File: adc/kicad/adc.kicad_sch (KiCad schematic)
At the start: 115 parts, among them J1 Conn_01x07_Pin, J2 Conn_01x02_Pin, J3 Conn_01x02_Pin, J4 Conn_01x02_Pin, J5 pcie_98, U1 ADS1261BIRHBT, U2 ESD5344D-TP, U3 TPS7A2050PDBVR, U4 TPS7A2025PDBVRr, U6 TPS65135, U7 ADP7182AUJZ-5.0, U8 ADP7182AUJZ-2.5, U9 XC6206P332MR

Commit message: Replaced ADC DC/DC inductor with a higher current one.
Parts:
- L1: footprint Inductor_SMD:L_0805_2012Metric -> adc:Inductor_C329578; LCSC C531291 -> C329578
- R23, R24: value 5K1 -> 10K; LCSC C25905 -> C25744
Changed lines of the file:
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@@
       (effects (font (size 1.27 1.27)))
     )
-    (property "Value" "5K1" (at 269.24 113.665 0)
+    (property "Value" "10K" (at 269.24 113.665 0)
       (effects (font (size 1.27 1.27)))
     )
@@
       (effects (font (size 1.27 1.27)) hide)
     )
-    (property "LCSC" "C25905" (at 272.415 112.395 0)
+    (property "LCSC" "C25744" (at 272.415 112.395 0)
       (effects (font (size 1.27 1.27)) hide)
     )
@@
       (effects (font (size 1.27 1.27)))
     )
-    (property "Value" "5K1" (at 287.02 113.665 0)
+    (property "Value" "10K" (at 287.02 113.665 0)
       (effects (font (size 1.27 1.27)))
     )
@@
       (effects (font (size 1.27 1.27)) hide)
     )
-    (property "LCSC" "C25905" (at 290.195 112.395 0)
+    (property "LCSC" "C25744" (at 290.195 112.395 0)
       (effects (font (size 1.27 1.27)) hide)
     )
@@
       (effects (font (size 1.27 1.27)))
     )
-    (property "Footprint" "Inductor_SMD:L_0805_2012Metric" (at 62.23 177.8 0)
+    (property "Footprint" "adc:Inductor_C329578" (at 62.23 177.8 0)
       (effects (font (size 1.27 1.27)) hide)
     )
@@
       (effects (font (size 1.27 1.27)) hide)
     )
-    (property "LCSC" "C531291" (at 62.23 177.8 90)
-      (effects (font (size 1.27 1.27)) hide)
-    )
+    (property "LCSC" "C329578" (at 62.23 177.8 90)
+      (effects (font (size 1.27 1.27)) hide)
+    )

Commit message: Updated JLCPCB part info and rotations.
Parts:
- J2, J3, J4, U7, U8, U9: JLCRotOffset (none) -> 180
- R31: LCSC C2759490 -> C4008631
- R33: LCSC C172084 -> C1861540
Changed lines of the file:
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@@
       (effects (font (size 1.27 1.27)) hide)
     )
-    (property "LCSC" "C2759490" (at 80.645 198.755 0)
+    (property "LCSC" "C4008631" (at 80.645 198.755 0)
       (effects (font (size 1.27 1.27)) hide)
     )
@@
       (effects (font (size 1.27 1.27)) hide)
     )
+    (property "JLCRotOffset" "180" (at 153.67 219.71 0)
+      (effects (font (size 1.27 1.27)) hide)
+    )
     (pin "1")
     (pin "2")
@@
       (effects (font (size 1.27 1.27)))
     )
+    (property "JLCRotOffset" "180" (at 284.48 186.69 0)
+      (effects (font (size 1.27 1.27)) hide)
+    )
     (pin "1")
     (pin "2")
@@
       (effects (font (size 1.27 1.27)) hide)
     )
-    (property "LCSC" "C172084" (at 80.645 213.36 0)
+    (property "LCSC" "C1861540" (at 80.645 213.36 0)
       (effects (font (size 1.27 1.27)) hide)
     )
@@
       (effects (font (size 1.27 1.27)) hide)
     )
+    (property "JLCRotOffset" "180" (at 187.96 48.895 0)
+      (effects (font (size 1.27 1.27)) hide)
+    )
     (pin "1")
     (pin "2")
@@
       (effects (font (size 1.27 1.27)) hide)
     )
+    (property "JLCRotOffset" "180" (at 124.46 48.895 0)
+      (effects (font (size 1.27 1.27)) hide)
+    )
     (pin "1")
     (pin "2")
@@
       (effects (font (size 1.27 1.27)) hide)
     )
+    (property "JLCRotOffset" "180" (at 250.825 48.895 0)
+      (effects (font (size 1.27 1.27)) hide)
+    )
     (pin "1")
     (pin "2")
@@
       (effects (font (size 1.27 1.27)) hide)
     )
+    (property "JLCRotOffset" "180" (at 201.295 219.71 0)
+      (effects (font (size 1.27 1.27)) hide)
+    )

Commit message: Fixed library pathes and bus pin number.
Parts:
- R33: LCSC C1861540 -> C4035752
- TP1, TP2, TP3, TP4, TP5, TP6, TP7, TP8, TP9: symbol Connector:TestPoint -> common:TestPoint
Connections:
- net PB14: now also J5.A16 (Pin_a16); no longer J5.B14 (Pin_b14)
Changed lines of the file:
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@@
   (no_connect (at 347.345 184.15))
   (no_connect (at 334.645 153.67))
-  (no_connect (at 347.345 100.33))
+  (no_connect (at 334.645 95.25))
   (no_connect (at 347.345 171.45))
   (no_connect (at 78.74 79.375))
@@
     (stroke (width 0) (type default))
   )
-  (wire (pts (xy 323.215 95.25) (xy 334.645 95.25))
+  (wire (pts (xy 347.345 100.33) (xy 357.505 100.33))
     (stroke (width 0) (type default))
   )
@@
     (effects (font (size 1.27 1.27)) (justify left bottom))
   )
-  (label "PB14" (at 323.215 95.25 0) (fields_autoplaced)
-    (effects (font (size 1.27 1.27)) (justify left bottom))
+  (label "PB14" (at 357.505 100.33 180) (fields_autoplaced)
+    (effects (font (size 1.27 1.27)) (justify right bottom))
   )
   (label "-2V5A" (at 55.88 149.86 90) (fields_autoplaced)
@@
     )
   )
-  (symbol (lib_id "Connector:TestPoint") (at 227.33 170.18 0) (unit 1)
+  (symbol (lib_id "common:TestPoint") (at 227.33 170.18 0) (unit 1)
     (in_bom no) (on_board yes) (dnp no)
     (property "Reference" "TP7" (at 226.06 164.465 0)
@@
       (effects (font (size 1.27 1.27)) hide)
     )
-    (property "LCSC" "C1861540" (at 80.645 213.36 0)
+    (property "LCSC" "C4035752" (at 80.645 213.36 0)
       (effects (font (size 1.27 1.27)) hide)
     )
@@
     )
   )
-  (symbol (lib_id "Connector:TestPoint") (at 227.33 222.25 180) (unit 1)
+  (symbol (lib_id "common:TestPoint") (at 227.33 222.25 180) (unit 1)
     (in_bom no) (on_board yes) (dnp no)
     (property "Reference" "TP8" (at 228.6 227.965 0)
@@
     )
   )
-  (symbol (lib_id "Connector:TestPoint") (at 33.655 193.675 0) (unit 1)
+  (symbol (lib_id "common:TestPoint") (at 33.655 193.675 0) (unit 1)
     (in_bom no) (on_board yes) (dnp no)
     (property "Reference" "TP2" (at 32.385 187.96 0)
@@
     )
   )
-  (symbol (lib_id "Connector:TestPoint") (at 93.98 218.44 180) (unit 1)
+  (symbol (lib_id "common:TestPoint") (at 93.98 218.44 180) (unit 1)
     (in_bom no) (on_board yes) (dnp no)
     (property "Reference" "TP4" (at 95.25 224.155 0)
@@
     )
   )
-  (symbol (lib_id "Connector:TestPoint") (at 299.72 184.15 0) (unit 1)
+  (symbol (lib_id "common:TestPoint") (at 299.72 184.15 0) (unit 1)
     (in_bom no) (on_board yes) (dnp no)
     (property "Reference" "TP9" (at 298.45 178.435 0)
@@
     )
   )
-  (symbol (lib_id "Connector:TestPoint") (at 174.625 222.25 180) (unit 1)
+  (symbol (lib_id "common:TestPoint") (at 174.625 222.25 180) (unit 1)
     (in_bom no) (on_board yes) (dnp no)
     (property "Reference" "TP6" (at 175.895 227.965 0)
@@
     )
   )
-  (symbol (lib_id "Connector:TestPoint") (at 259.715 155.575 0) (unit 1)
+  (symbol (lib_id "common:TestPoint") (at 259.715 155.575 0) (unit 1)
     (in_bom no) (on_board yes) (dnp no)
     (property "Reference" "TP1" (at 258.445 149.86 0)
@@
     )
   )
-  (symbol (lib_id "Connector:TestPoint") (at 174.625 170.18 0) (unit 1)
+  (symbol (lib_id "common:TestPoint") (at 174.625 170.18 0) (unit 1)
     (in_bom no) (on_board yes) (dnp no)
     (property "Reference" "TP5" (at 173.355 164.465 0)
@@
     )
   )
-  (symbol (lib_id "Connector:TestPoint") (at 93.98 194.31 0) (unit 1)
+  (symbol (lib_id "common:TestPoint") (at 93.98 194.31 0) (unit 1)
     (in_bom no) (on_board yes) (dnp no)
     (property "Reference" "TP3" (at 92.71 188.595 0)

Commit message: Changed LED to green and used DC/DC footprint with longer pads for manual soldering.
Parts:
- D1, D2, D3, D4, D5: LCSC C2286 -> C72043
- U6: footprint Package_DFN_QFN:WQFN-16-1EP_3x3mm_P0.5mm_EP1.68x1.68mm_ThermalVias -> adc:WQFN-16-1EP_3x3mm_P0.5mm_EP1.68x1.68mm_ThermalVias
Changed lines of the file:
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@@
       (effects (font (size 1.27 1.27)) hide)
     )
-    (property "LCSC" "C2286" (at 299.72 121.285 0)
+    (property "LCSC" "C72043" (at 299.72 121.285 0)
       (effects (font (size 1.27 1.27)) hide)
     )
@@
       (effects (font (size 1.27 1.27)) hide)
     )
-    (property "LCSC" "C2286" (at 290.195 121.285 0)
+    (property "LCSC" "C72043" (at 290.195 121.285 0)
       (effects (font (size 1.27 1.27)) hide)
     )
@@
       (effects (font (size 1.27 1.27)))
     )
-    (property "Footprint" "Package_DFN_QFN:WQFN-16-1EP_3x3mm_P0.5mm_EP1.68x1.68mm_ThermalVias" (at 39.37 166.37 0)
+    (property "Footprint" "adc:WQFN-16-1EP_3x3mm_P0.5mm_EP1.68x1.68mm_ThermalVias" (at 39.37 166.37 0)
       (effects (font (size 1.27 1.27)) hide)
     )
@@
       (effects (font (size 1.27 1.27)) hide)
     )
-    (property "LCSC" "C2286" (at 272.415 120.015 0)
+    (property "LCSC" "C72043" (at 272.415 120.015 0)
       (effects (font (size 1.27 1.27)) hide)
     )
@@
       (effects (font (size 1.27 1.27)) hide)
     )
-    (property "LCSC" "C2286" (at 263.525 120.015 0)
+    (property "LCSC" "C72043" (at 263.525 120.015 0)
       (effects (font (size 1.27 1.27)) hide)
     )
@@
       (effects (font (size 1.27 1.27)) hide)
     )
-    (property "LCSC" "C2286" (at 281.305 120.015 0)
+    (property "LCSC" "C72043" (at 281.305 120.015 0)
       (effects (font (size 1.27 1.27)) hide)
     )

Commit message: Changed ADC LEDs values from RED to GRN.
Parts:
- D1, D2, D3, D4, D5: value RED -> GRN
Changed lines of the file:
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@@
       (effects (font (size 1.27 1.27)) (justify right))
     )
-    (property "Value" "RED" (at 305.435 118.745 90)
+    (property "Value" "GRN" (at 305.435 118.745 90)
       (effects (font (size 1.27 1.27)) (justify right))
     )
@@
       (effects (font (size 1.27 1.27)) (justify right))
     )
-    (property "Value" "RED" (at 295.91 118.745 90)
+    (property "Value" "GRN" (at 295.91 118.745 90)
       (effects (font (size 1.27 1.27)) (justify right))
     )
@@
       (effects (font (size 1.27 1.27)) (justify right))
     )
-    (property "Value" "RED" (at 266.7 122.555 90)
+    (property "Value" "GRN" (at 266.7 122.555 90)
       (effects (font (size 1.27 1.27)) (justify right))
     )
@@
       (effects (font (size 1.27 1.27)) (justify right))
     )
-    (property "Value" "RED" (at 257.81 122.555 90)
+    (property "Value" "GRN" (at 257.81 122.555 90)
       (effects (font (size 1.27 1.27)) (justify right))
     )
@@
       (effects (font (size 1.27 1.27)) (justify right))
     )
-    (property "Value" "RED" (at 275.59 122.555 90)
+    (property "Value" "GRN" (at 275.59 122.555 90)
       (effects (font (size 1.27 1.27)) (justify right))
     )

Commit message: Minor tweak of the schematics.
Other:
- note added: "TODO: Merge grounds"
- note added: "TODO: Swap the supply and sense pins of the load cell connector."
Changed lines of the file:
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@@
     (effects (font (size 1.27 1.27)) (justify left bottom))
+  )
+  (text "TODO: Swap the supply and sense pins of the load cell connector."
+    (at 21.59 20.32 0)
+    (effects (font (size 2.54 2.54) (thickness 0.508) bold (color 255 0 0 1)) (justify left bottom))
+  )
+  (text "TODO: Merge grounds" (at 22.225 28.575 0)
+    (effects (font (size 2.54 2.54) (thickness 0.508) bold (color 255 0 0 1)) (justify left bottom))
   )
   (text "MEASURED (AIN6-AIN7)/(AVDD-AVSS)" (at 192.405 74.93 0)

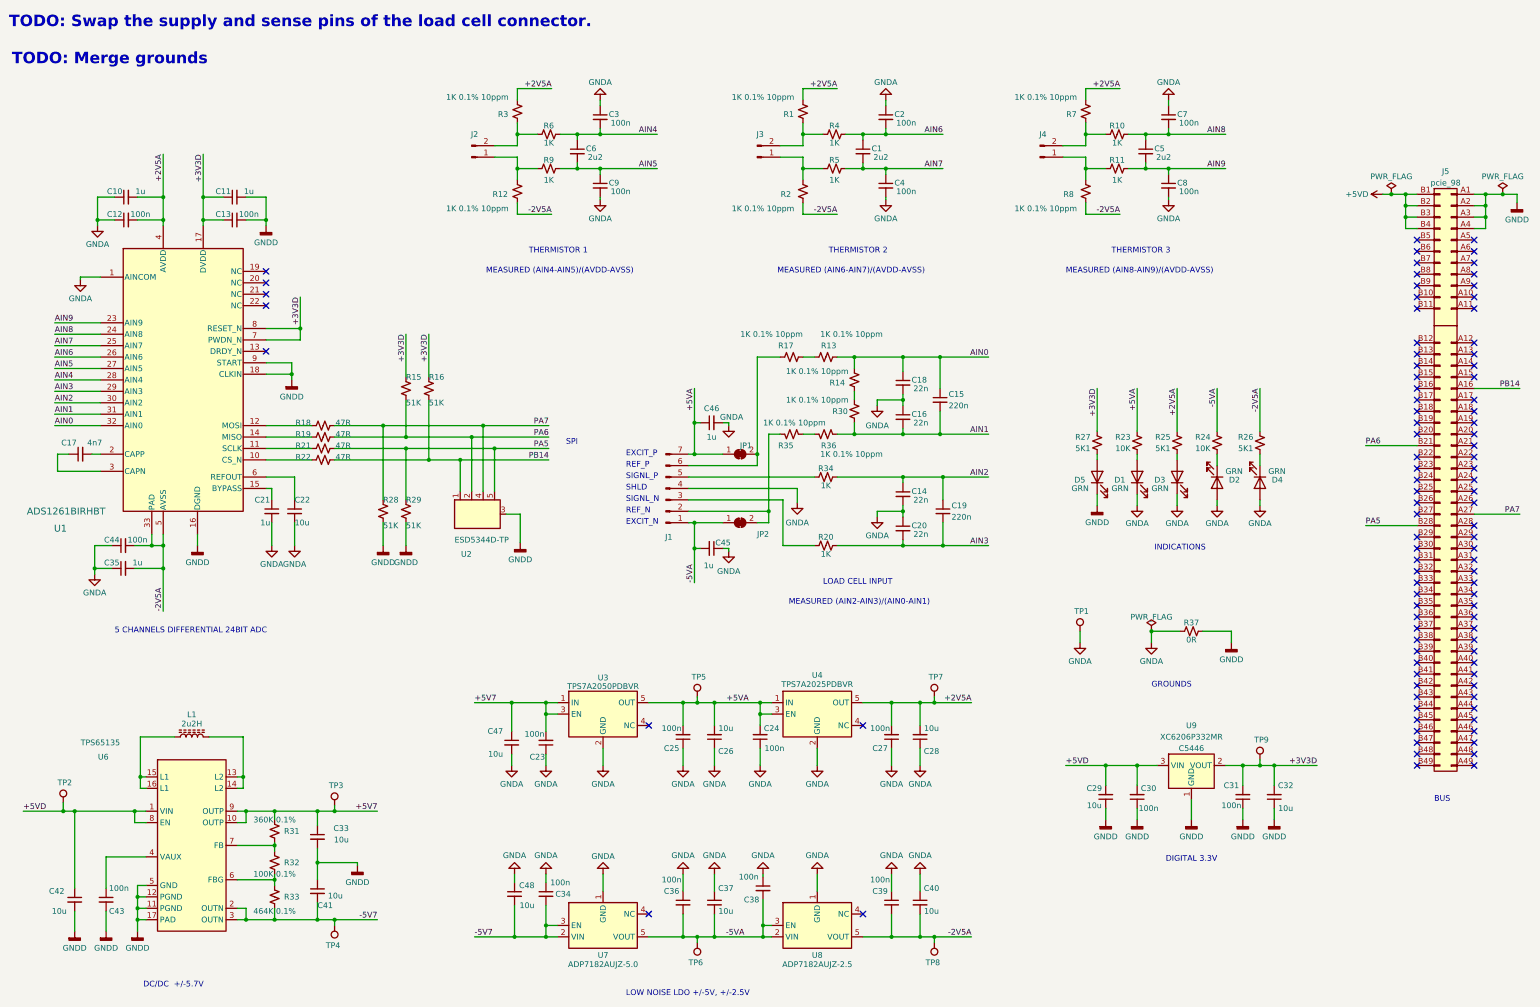
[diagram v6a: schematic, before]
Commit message: Clenaed up ADC TODOs. Changed DC/DC resistors from 0.1% to 1% and merged grounds.
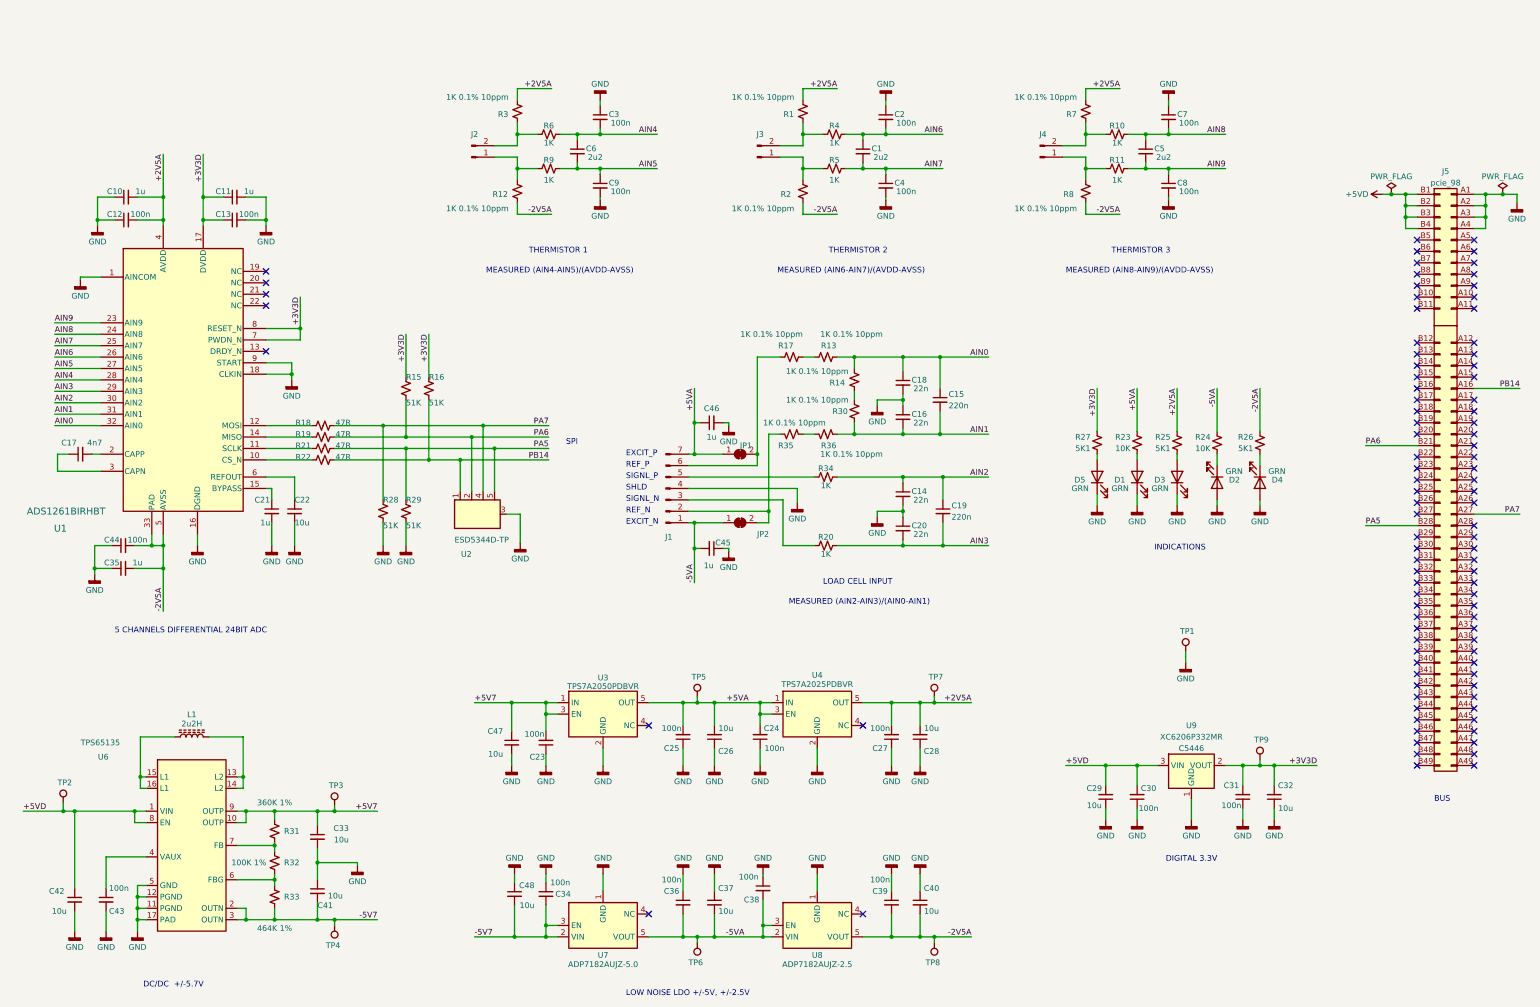
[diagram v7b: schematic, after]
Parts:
- removed R37: 0R, Resistor_SMD:R_0805_2012Metric, symbol Device:R_Small_US
- R31: value 360K 0.1% -> 360K 1%; LCSC C4008631 -> C308007
- R32: value 100K 0.1% -> 100K 1%; LCSC C852328 -> C25741
- R33: value 464K 0.1% -> 464K 1%; LCSC C4035752 -> C477740
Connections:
- net GNDD is gone; now on net GND: C11.2, C13.2, C29.1, C30.1, C31.1, C32.1, C33.2, C41.1, C42.2, C43.2, D5.1 (K), J5.A1 (Pin_a1), J5.A2 (Pin_a2), J5.A3 (Pin_a3), J5.A4 (Pin_a4), R28.1, R29.1, U1.16 (DGND), U1.18 (CLKIN), U1.9 (START), U2.3 (GND), U6.11 (PGND), U6.12 (PGND), U6.17 (PAD), U6.5 (GND), U9.1 (GND)
- net GNDA renamed GND
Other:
- note removed: "GROUNDS"
- note removed: "TODO: Merge grounds"
- note removed: "TODO: Swap the supply and sense pins of the load cell connector."
- moved on the sheet: TP1

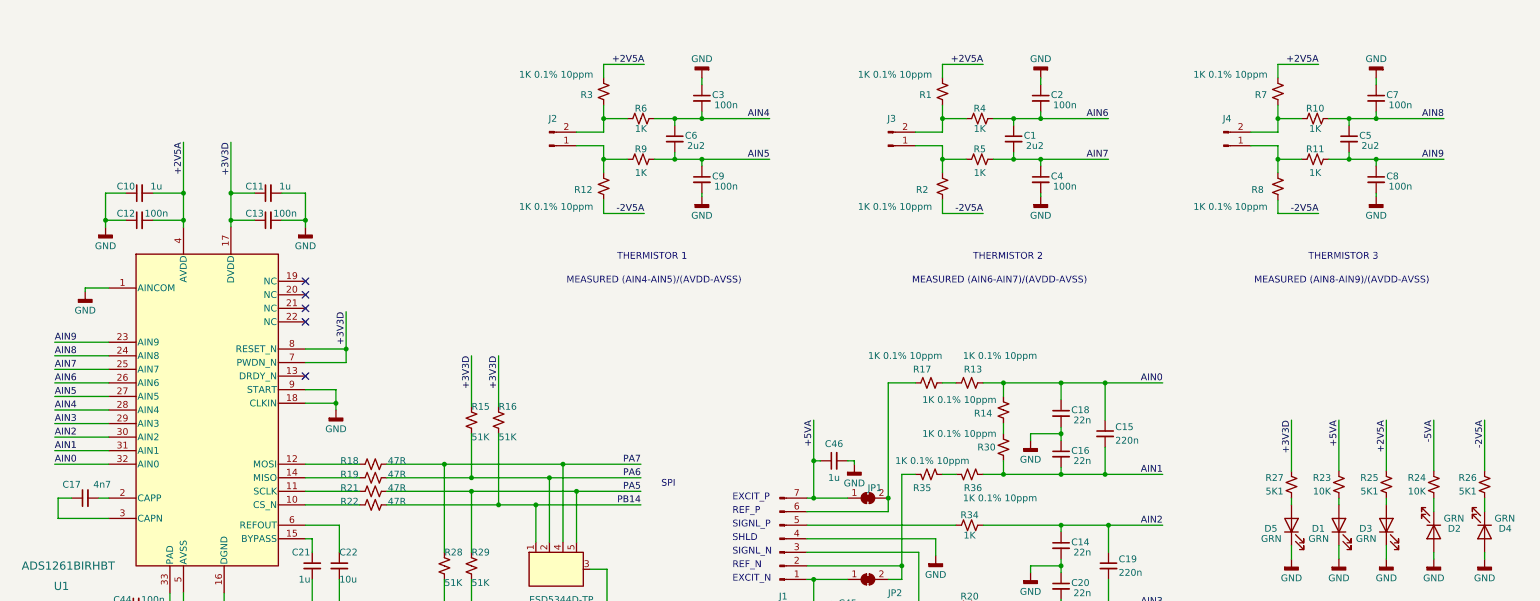
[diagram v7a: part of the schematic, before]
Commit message: Updated the thermistor inputs to use 2K voltage divider.
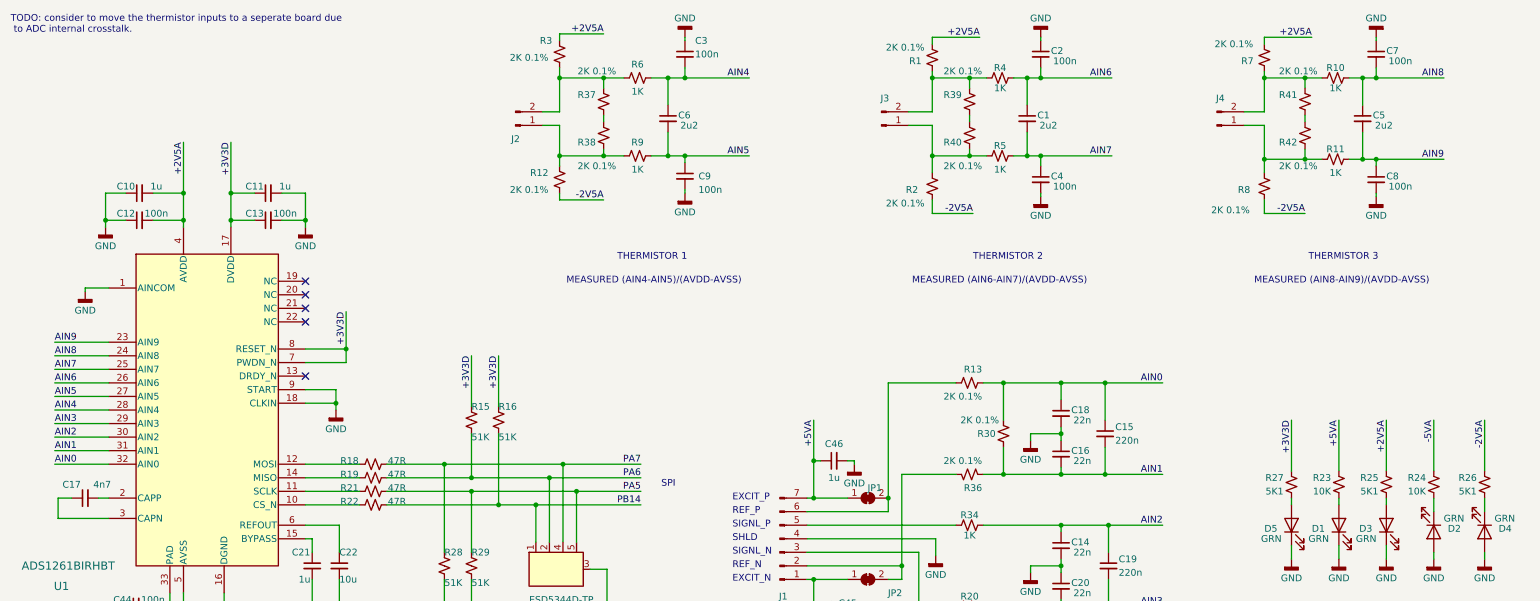
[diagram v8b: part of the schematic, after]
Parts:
- removed R14, R17, R35: 1K 0.1% 10ppm, Resistor_SMD:R_0402_1005Metric, symbol Device:R_Small_US
- added R37, R38, R39, R40, R41, R42: 2K 0.1%, Resistor_SMD:R_0402_1005Metric, symbol Device:R_Small_US
- R1, R12, R13, R2, R3, R30, R36, R7: value 1K 0.1% 10ppm -> 2K 0.1%; LCSC C328418 -> C852711
- R8: value 1K 0.1% 10ppm -> 2K 0.1%
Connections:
- net AIN0: now also R30.2
- net at J2.1 (Pin_1), R12.2, R9.1: now also R38.1
- net at J3.1 (Pin_1), R2.2, R5.1: now also R40.1
- net at J3.2 (Pin_2), R1.1, R4.1: now also R39.2
- net at R36.2: now also J1.2 (Pin_2), JP2.2 (B)
- net at J2.2 (Pin_2), R3.1, R6.1: now also R37.2
- net at J4.2 (Pin_2), R10.1, R7.1: now also R41.2
- net at J1.6 (Pin_6), JP1.2 (B): now also R13.2
- net at J4.1 (Pin_1), R11.1, R8.2: now also R42.1
- new net: R39.1, R40.2
- new net: R37.1, R38.2
- new net: R41.1, R42.2
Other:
- note added: "TODO: consider to move the thermistor inputs to a seperate board due to ADC internal crosstalk."
- moved on the sheet: C1, C2, C3, C5, C6, C7, C9, J2, J3, J4, R1, R10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
